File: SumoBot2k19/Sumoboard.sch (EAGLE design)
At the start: 38 parts

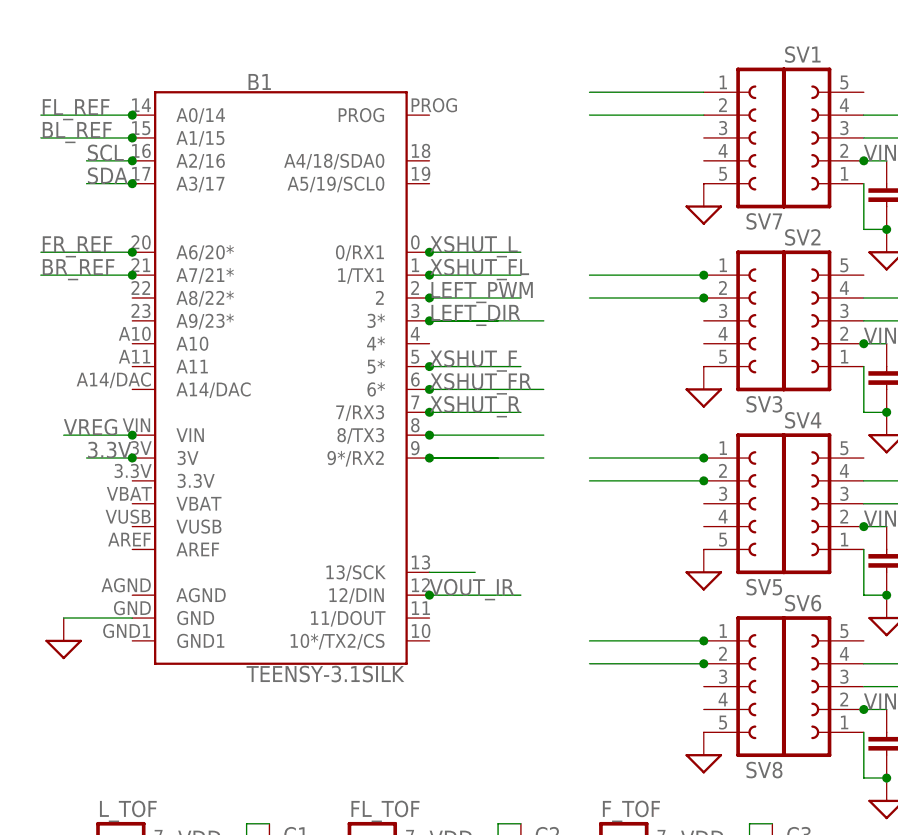
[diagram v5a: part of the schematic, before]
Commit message: modified TOF, motor driver airway connetions; moved some components around
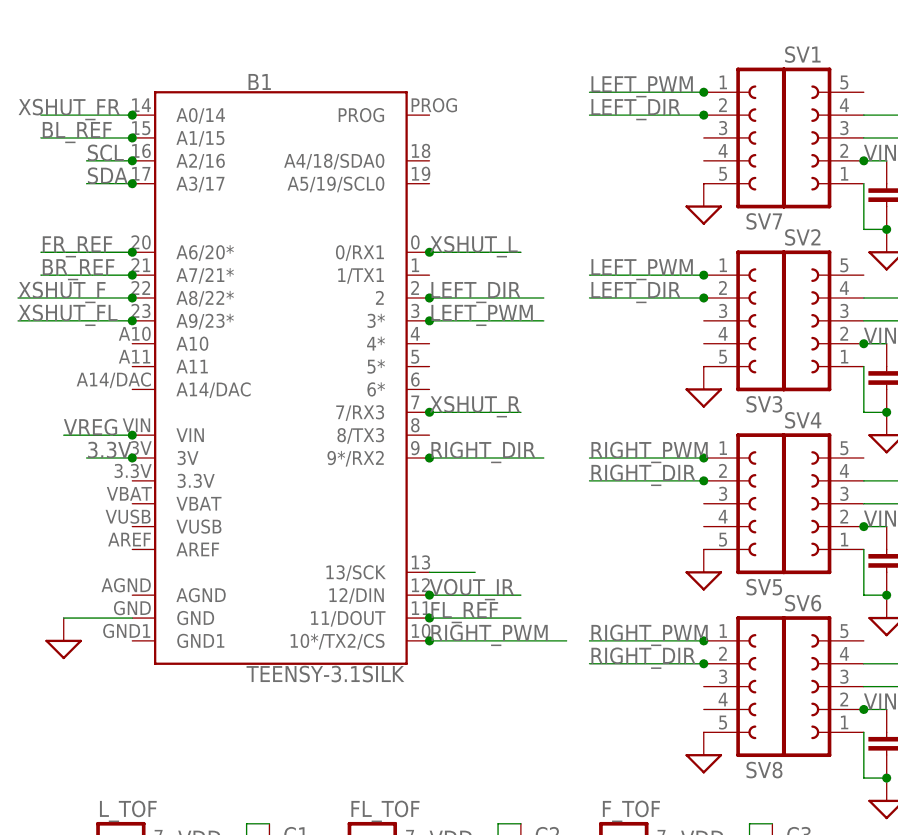
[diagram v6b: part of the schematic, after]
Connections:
- net FL_REF: now also B1.11/DOUT; no longer B1.A0/14
- net LEFT_DIR: now also B1.2; no longer B1.9*/RX2
- net LEFT_PWM: now also B1.3*; no longer B1.8/TX3
- net RIGHT_DIR: now also B1.9*/RX2; no longer B1.3*
- net RIGHT_PWM: now also B1.10*/TX2/CS; no longer B1.2
- net XSHUT_F: now also B1.A8/22*; no longer B1.5*
- net XSHUT_FL: now also B1.A9/23*; no longer B1.1/TX1
- net XSHUT_FR: now also B1.A0/14; no longer B1.6*
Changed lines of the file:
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@@
 <setting verticaltext="up"/>
 </settings>
-<grid distance="0.1" unitdist="inch" unit="inch" style="lines" multiple="1" display="yes" altdistance="0.01" altunitdist="inch" altunit="inch"/>
+<grid distance="0.1" unitdist="inch" unit="inch" style="lines" multiple="1" display="no" altdistance="0.01" altunitdist="inch" altunit="inch"/>
 <layers>
 <layer number="1" name="Top" color="4" fill="1" visible="no" active="no"/>
@@
 </segment>
 <segment>
-<pinref part="B1" gate="G$1" pin="1/TX1"/>
-<junction x="30.48" y="83.82"/>
-<label x="30.48" y="83.82" size="1.778" layer="95"/>
-<wire x1="40.64" y1="83.82" x2="30.48" y2="83.82" width="0.1524" layer="91"/>
+<pinref part="B1" gate="G$1" pin="A9/23*"/>
+<junction x="-2.54" y="78.74"/>
+<wire x1="-15.24" y1="78.74" x2="-2.54" y2="78.74" width="0.1524" layer="91"/>
+<label x="-15.24" y="78.74" size="1.778" layer="95"/>
 </segment>
 </net>
@@
 </segment>
 <segment>
-<pinref part="B1" gate="G$1" pin="5*"/>
-<junction x="30.48" y="73.66"/>
-<label x="30.48" y="73.66" size="1.778" layer="95"/>
-<wire x1="40.64" y1="73.66" x2="30.48" y2="73.66" width="0.1524" layer="91"/>
+<pinref part="B1" gate="G$1" pin="A8/22*"/>
+<junction x="-2.54" y="81.28"/>
+<label x="-15.24" y="81.28" size="1.778" layer="95"/>
+<wire x1="-15.24" y1="81.28" x2="-2.54" y2="81.28" width="0.1524" layer="91"/>
 </segment>
 </net>
@@
 </segment>
 <segment>
-<pinref part="B1" gate="G$1" pin="6*"/>
-<junction x="30.48" y="71.12"/>
-<label x="30.48" y="71.12" size="1.778" layer="95"/>
-<wire x1="43.18" y1="71.12" x2="30.48" y2="71.12" width="0.1524" layer="91"/>
+<pinref part="B1" gate="G$1" pin="A0/14"/>
+<junction x="-2.54" y="101.6"/>
+<label x="-15.24" y="101.6" size="1.778" layer="95"/>
+<wire x1="-12.7" y1="101.6" x2="-2.54" y2="101.6" width="0.1524" layer="91"/>
 </segment>
 </net>
@@
 <net name="FL_REF" class="0">
 <segment>
-<pinref part="B1" gate="G$1" pin="A0/14"/>
-<junction x="-2.54" y="101.6"/>
-<label x="-12.7" y="101.6" size="1.778" layer="95"/>
-<wire x1="-12.7" y1="101.6" x2="-2.54" y2="101.6" width="0.1524" layer="91"/>
-</segment>
-<segment>
 <pinref part="FL_REF" gate="J$1" pin="3"/>
 <junction x="149.86" y="91.44"/>
 <label x="149.86" y="91.44" size="1.778" layer="95"/>
+</segment>
+<segment>
+<pinref part="B1" gate="G$1" pin="11/DOUT"/>
+<junction x="30.48" y="45.72"/>
+<wire x1="30.48" y1="45.72" x2="40.64" y2="45.72" width="0.1524" layer="91"/>
+<label x="30.48" y="45.72" size="1.778" layer="95"/>
 </segment>
 </net>
@@
 <junction x="60.96" y="60.96"/>
 <wire x1="48.26" y1="60.96" x2="60.96" y2="60.96" width="0.1524" layer="91"/>
+<label x="48.26" y="60.96" size="1.778" layer="95"/>
 </segment>
 <segment>
@@
 <junction x="60.96" y="40.64"/>
 <wire x1="48.26" y1="40.64" x2="60.96" y2="40.64" width="0.1524" layer="91"/>
-</segment>
-<segment>
-<pinref part="B1" gate="G$1" pin="3*"/>
-<junction x="30.48" y="78.74"/>
-<wire x1="38.1" y1="78.74" x2="30.48" y2="78.74" width="0.1524" layer="91"/>
-<wire x1="43.18" y1="78.74" x2="30.48" y2="78.74" width="0.1524" layer="91"/>
+<label x="48.26" y="40.64" size="1.778" layer="95"/>
+</segment>
+<segment>
+<pinref part="B1" gate="G$1" pin="9*/RX2"/>
+<junction x="30.48" y="63.5"/>
+<label x="30.48" y="63.5" size="1.778" layer="95"/>
+<wire x1="30.48" y1="63.5" x2="43.18" y2="63.5" width="0.1524" layer="91"/>
 </segment>
 </net>
@@
 <pinref part="SV7" gate="G$1" pin="2"/>
 <wire x1="60.96" y1="101.6" x2="48.26" y2="101.6" width="0.1524" layer="91"/>
+<junction x="60.96" y="101.6"/>
+<label x="48.26" y="101.6" size="1.778" layer="95"/>
 </segment>
 <segment>
@@
 <junction x="60.96" y="81.28"/>
 <wire x1="48.26" y1="81.28" x2="60.96" y2="81.28" width="0.1524" layer="91"/>
-</segment>
-<segment>
-<pinref part="B1" gate="G$1" pin="9*/RX2"/>
-<label x="30.48" y="78.74" size="1.778" layer="95"/>
-<wire x1="38.1" y1="63.5" x2="30.48" y2="63.5" width="0.1524" layer="91"/>
-<junction x="30.48" y="63.5"/>
-<wire x1="30.48" y1="63.5" x2="43.18" y2="63.5" width="0.1524" layer="91"/>
+<label x="48.26" y="81.28" size="1.778" layer="95"/>
+</segment>
+<segment>
+<pinref part="B1" gate="G$1" pin="2"/>
+<junction x="30.48" y="81.28"/>
+<label x="30.48" y="81.28" size="1.778" layer="95"/>
+<wire x1="30.48" y1="81.28" x2="43.18" y2="81.28" width="0.1524" layer="91"/>
 </segment>
 </net>
@@
 <pinref part="SV7" gate="G$1" pin="1"/>
 <wire x1="48.26" y1="104.14" x2="60.96" y2="104.14" width="0.1524" layer="91"/>
+<junction x="60.96" y="104.14"/>
+<label x="48.26" y="104.14" size="1.778" layer="95"/>
 </segment>
 <segment>
@@
 <junction x="60.96" y="83.82"/>
 <wire x1="48.26" y1="83.82" x2="60.96" y2="83.82" width="0.1524" layer="91"/>
-</segment>
-<segment>
-<pinref part="B1" gate="G$1" pin="8/TX3"/>
-<label x="30.48" y="81.28" size="1.778" layer="95"/>
-<wire x1="43.18" y1="66.04" x2="30.48" y2="66.04" width="0.1524" layer="91"/>
-<junction x="30.48" y="66.04"/>
+<label x="48.26" y="83.82" size="1.778" layer="95"/>
+</segment>
+<segment>
+<pinref part="B1" gate="G$1" pin="3*"/>
+<junction x="30.48" y="78.74"/>
+<label x="30.48" y="78.74" size="1.778" layer="95"/>
+<wire x1="30.48" y1="78.74" x2="43.18" y2="78.74" width="0.1524" layer="91"/>
 </segment>
 </net>
@@
 <junction x="60.96" y="63.5"/>
 <wire x1="48.26" y1="63.5" x2="60.96" y2="63.5" width="0.1524" layer="91"/>
+<label x="48.26" y="63.5" size="1.778" layer="95"/>
 </segment>
 <segment>
@@
 <junction x="60.96" y="43.18"/>
 <wire x1="48.26" y1="43.18" x2="60.96" y2="43.18" width="0.1524" layer="91"/>
-</segment>
-<segment>
-<pinref part="B1" gate="G$1" pin="2"/>
-<junction x="30.48" y="81.28"/>
-<wire x1="40.64" y1="81.28" x2="30.48" y2="81.28" width="0.1524" layer="91"/>
-</segment>
-</net>
+<label x="48.26" y="43.18" size="1.778" layer="95"/>
+</segment>
+<segment>
+<pinref part="B1" gate="G$1" pin="10*/TX2/CS"/>
+<junction x="30.48" y="43.18"/>
+<label x="30.48" y="43.18" size="1.778" layer="95"/>
+<wire x1="30.48" y1="43.18" x2="45.72" y2="43.18" width="0.1524" layer="91"/>
+</segment>
+</net>

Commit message: more routes!!! :D
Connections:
- net BL_REF: now also B1.5*; no longer B1.A1/15
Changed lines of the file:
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@@
 <net name="BL_REF" class="0">
-<segment>
-<pinref part="B1" gate="G$1" pin="A1/15"/>
-<junction x="-2.54" y="99.06"/>
-<label x="-12.7" y="99.06" size="1.778" layer="95"/>
-<wire x1="-12.7" y1="99.06" x2="-2.54" y2="99.06" width="0.1524" layer="91"/>
-</segment>
 <segment>
 <pinref part="BL_REF" gate="J$1" pin="3"/>
@@
 <label x="172.72" y="88.9" size="1.778" layer="95"/>
 </segment>
+<segment>
+<pinref part="B1" gate="G$1" pin="5*"/>
+<junction x="30.48" y="73.66"/>
+<label x="30.48" y="73.66" size="1.778" layer="95"/>
+<wire x1="30.48" y1="73.66" x2="43.18" y2="73.66" width="0.1524" layer="91"/>
+</segment>
 </net>

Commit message: ripped
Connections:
- net VIN: now also SWITCH.3
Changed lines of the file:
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@@
 <junction x="139.7" y="40.64"/>
 <label x="139.7" y="40.64" size="1.778" layer="95"/>
+<pinref part="SWITCH" gate="J$1" pin="3"/>
+<wire x1="139.7" y1="43.18" x2="139.7" y2="40.64" width="0.1524" layer="91"/>
 </segment>
 </net>
